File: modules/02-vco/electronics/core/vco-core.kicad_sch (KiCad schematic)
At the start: 8 parts, among them J1 Conn_01x04, J2 Conn_02x05_Odd_Even, J6 Conn_02x02_Counter_Clockwise, J8 Conn_01x07

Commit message: VCO JLCPCB export done for v1.0
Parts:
- J6, J8: CHECKED YES -> (none)
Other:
- title: Hog Moduleur VCO core -> Moduleur VCO core
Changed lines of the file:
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@@
 	(paper "A4")
 	(title_block
-		(title "Hog Moduleur VCO core")
-		(date "2025-10-24")
-		(rev "v0.2")
+		(title "Moduleur VCO core")
+		(date "2025-12-11")
+		(rev "v1.0")
 		(company "Shmøergh")
 	)
@@
 			)
 		)
-		(property "CHECKED" "YES"
+		(property "CHECKED" ""
 			(at 255.27 101.6 0)
 			(effects
@@
 			)
 		)
-		(property "CHECKED" "YES"
+		(property "CHECKED" ""
 			(at 215.9 60.96 0)
 			(effects

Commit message: VCO JLCPCB export done for v1.0
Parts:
- J6: CHECKED (none) -> YES
- J8: Part URL https://mou.sr/40bhVZG -> (none)
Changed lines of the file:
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@@
 			)
 		)
-		(property "CHECKED" ""
+		(property "CHECKED" "YES"
 			(at 255.27 101.6 0)
 			(effects
@@
 			)
 		)
-		(property "Part URL" "https://mou.sr/40bhVZG"
+		(property "Part URL" ""
 			(at 215.9 60.96 0)
 			(effects

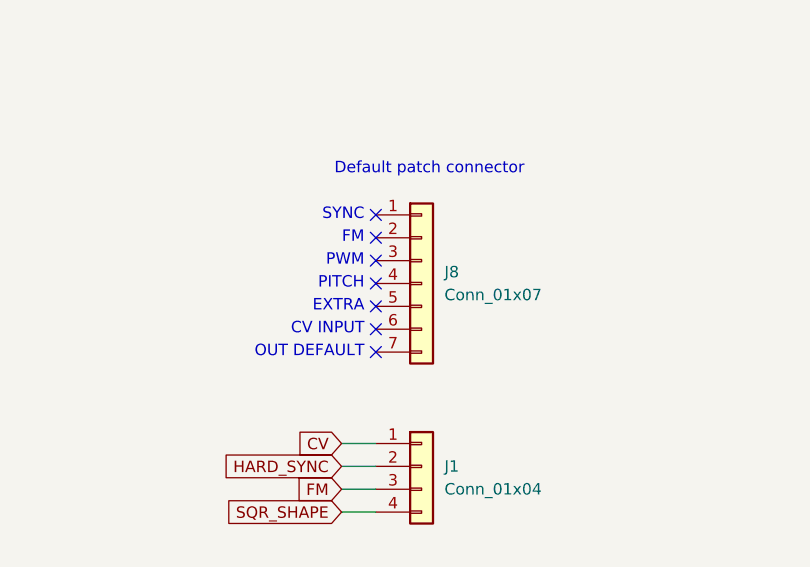
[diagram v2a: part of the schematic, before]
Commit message: Marked VCO core default holes as do-not-populate
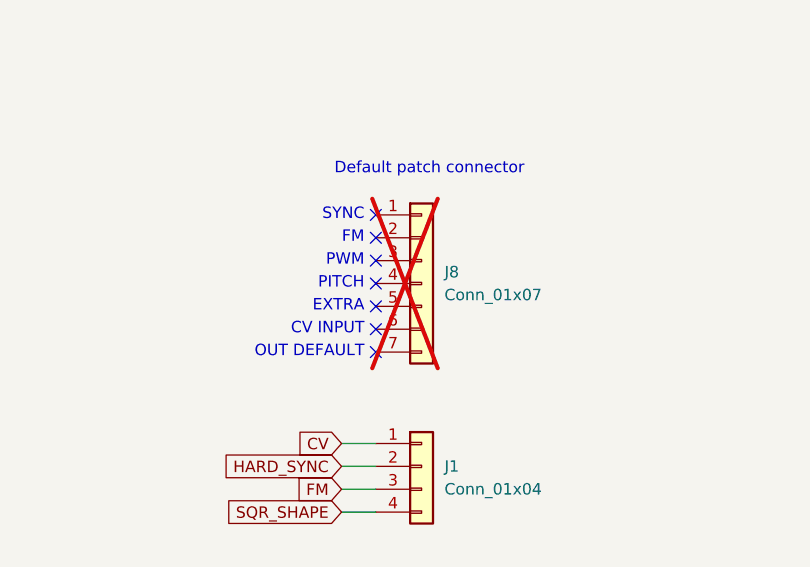
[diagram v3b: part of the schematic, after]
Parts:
- J8: now not fitted
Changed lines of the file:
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@@
 		(in_bom yes)
 		(on_board yes)
-		(dnp no)
+		(dnp yes)
 		(fields_autoplaced yes)
 		(property "Reference" "J8"
